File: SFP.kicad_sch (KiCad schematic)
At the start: 45 parts, among them J6 Bel-Fuse_SFP+_1x20_SS-79100-0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, U13 PCA9539AHF

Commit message: [#82757] Rename project to jetson-agx-thor-baseboard
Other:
- title: Jetson Orin AGX Baseboard -> Jetson AGX Thor Baseboard
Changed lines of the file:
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@@
 	(paper "A3")
 	(title_block
-		(title "Jetson Orin AGX Baseboard")
+		(title "Jetson AGX Thor Baseboard")
 		(date "2025-08-11")
 		(rev "1.0.0")

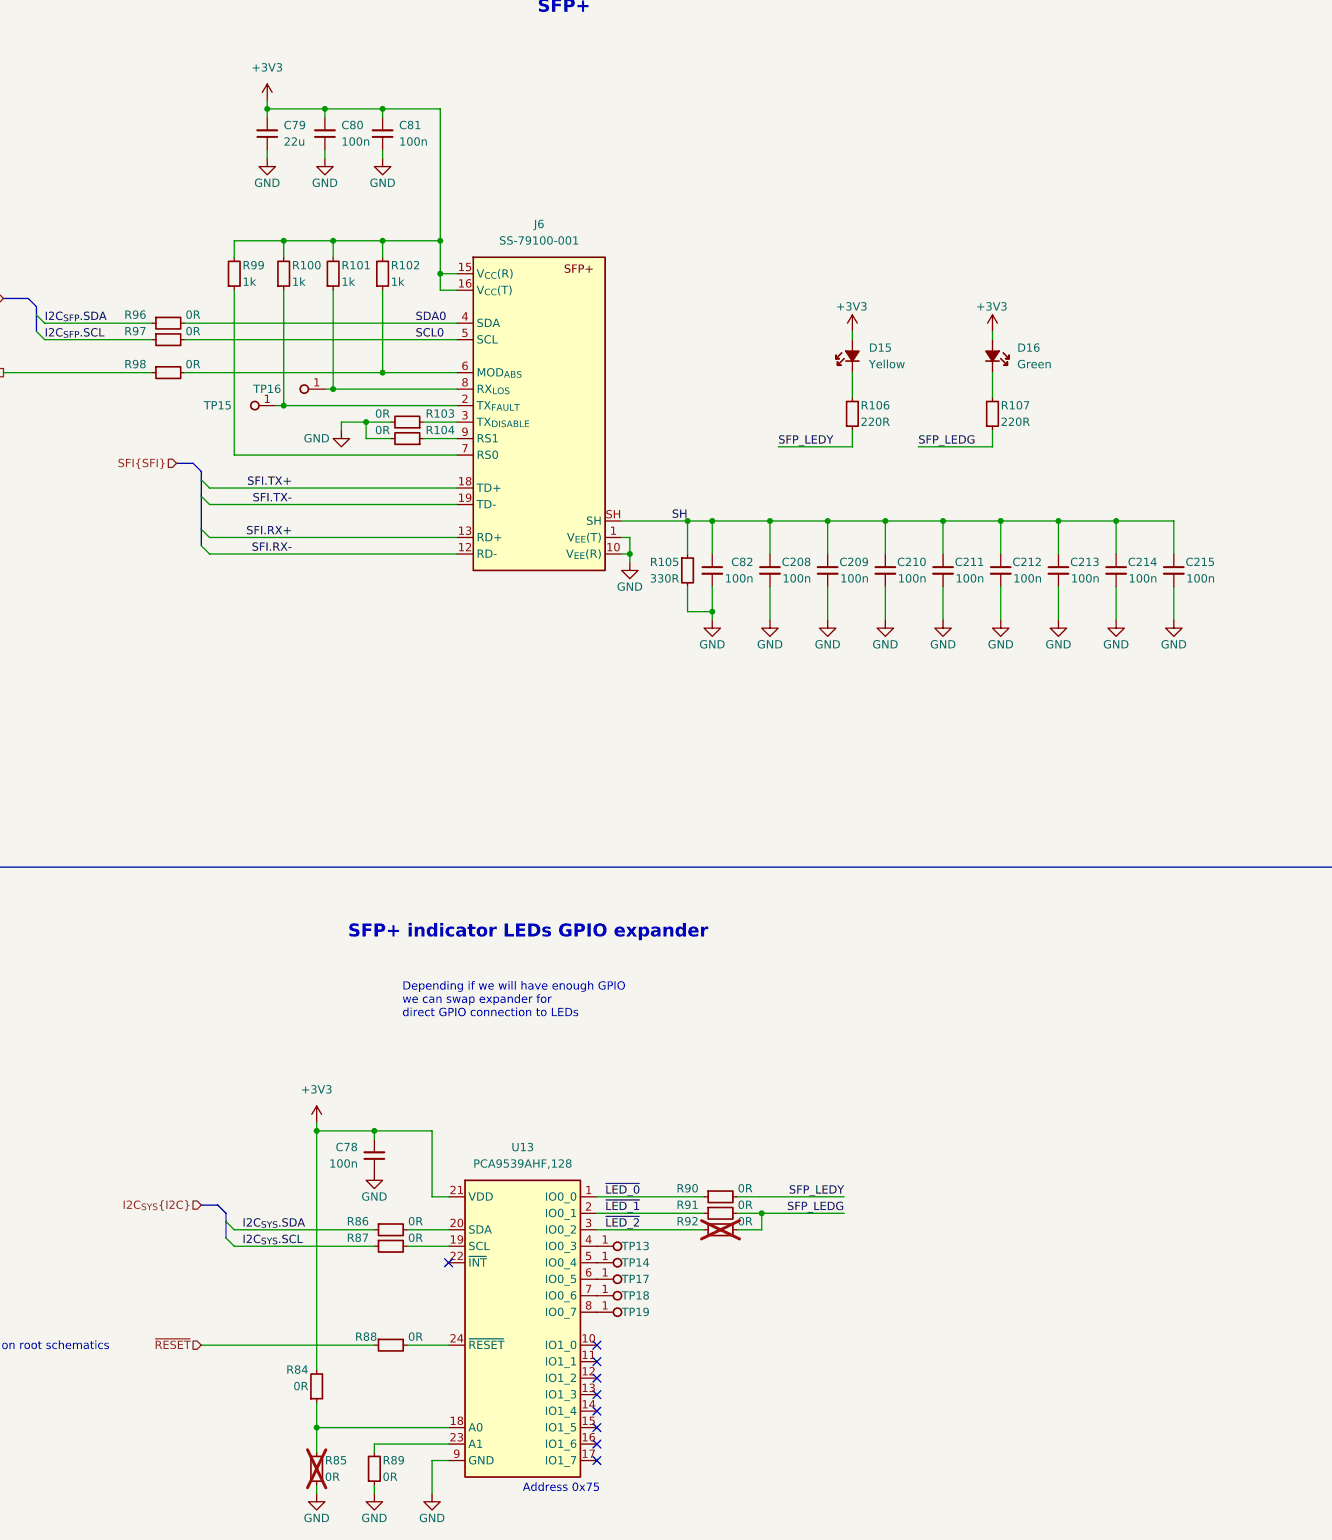
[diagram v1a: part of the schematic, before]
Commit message: [#82757] Cleanup: reorganise page numbers and fix annotations
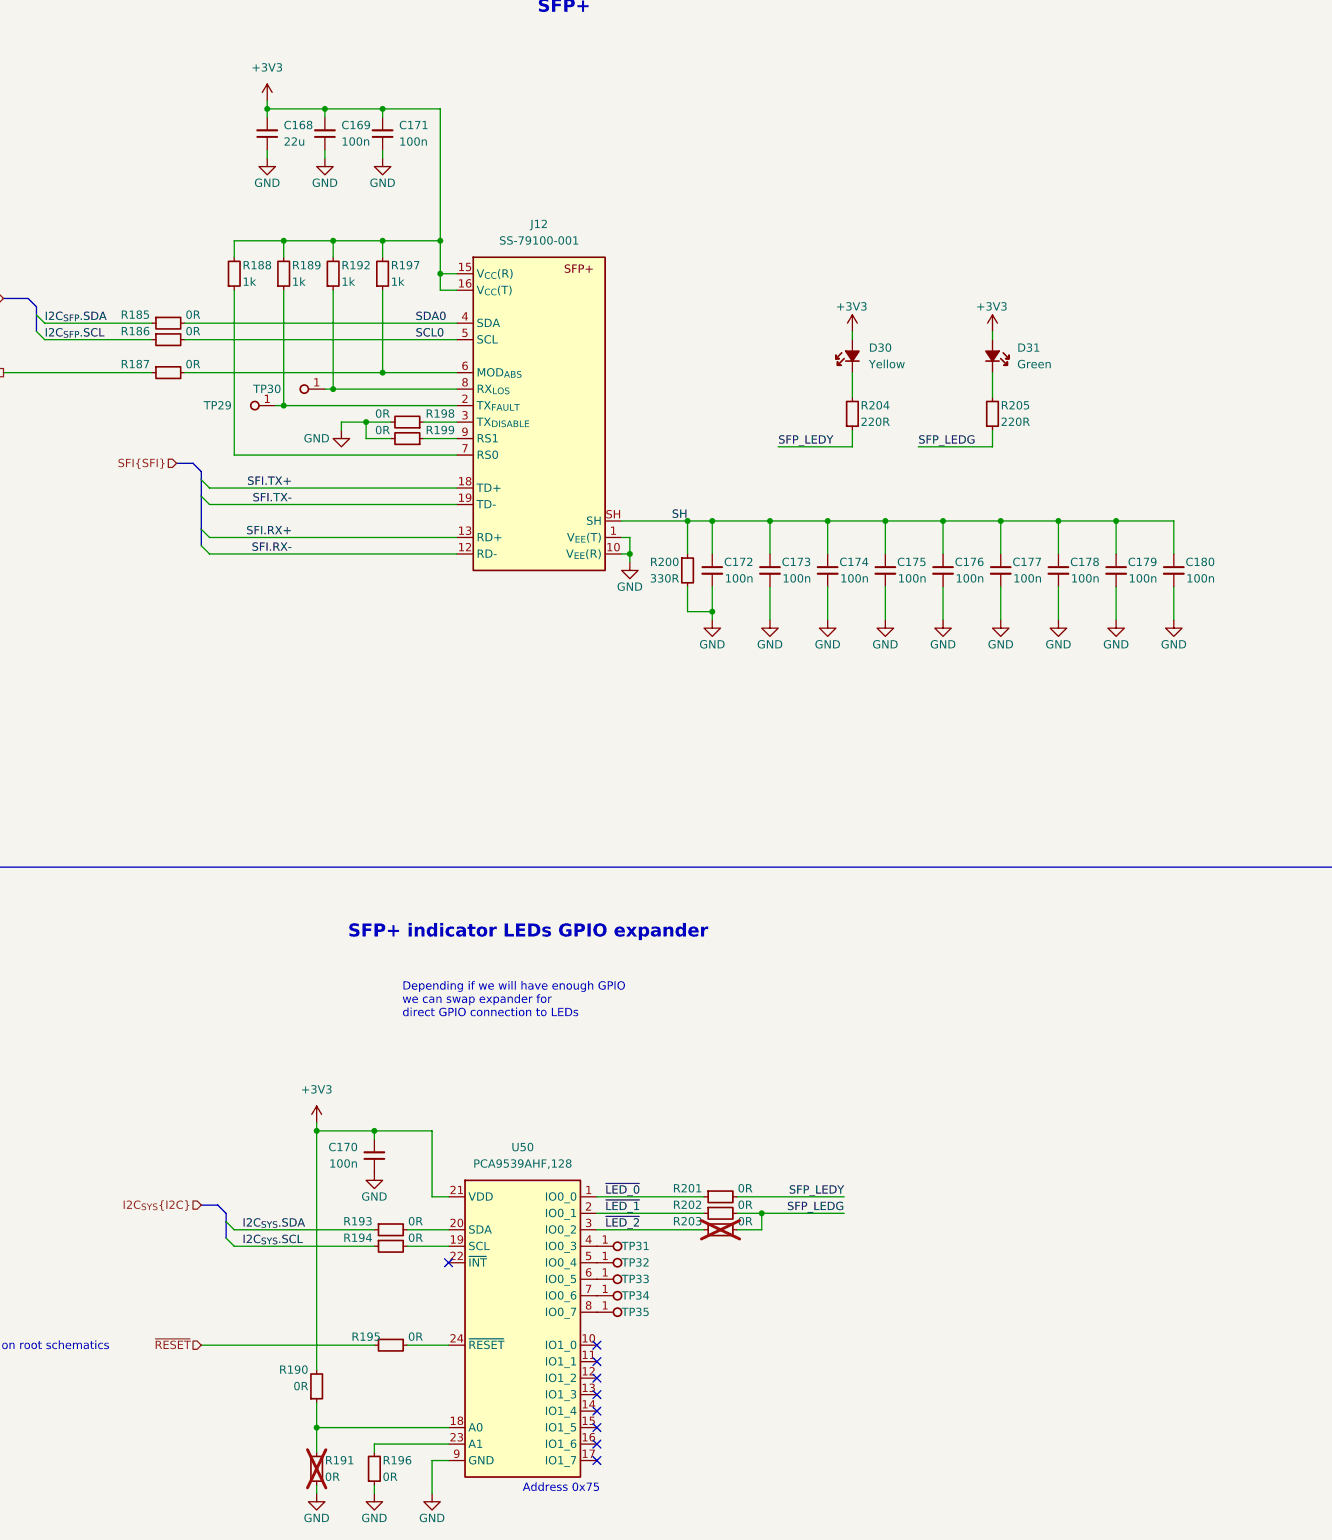
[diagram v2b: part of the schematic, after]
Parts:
- renumbered C79 to C168, C80 to C169, C78 to C170, C81 to C171, C82 to C172, C208 to C173, C209 to C174, C210 to C175, C211 to C176, C212 to C177, C213 to C178, C214 to C179, C215 to C180, D15 to D30, D16 to D31, J6 to J12, R96 to R185, R97 to R186, R98 to R187, R99 to R188, R100 to R189, R84 to R190, R85 to R191, R101 to R192, R86 to R193, R87 to R194, R88 to R195, R89 to R196, R102 to R197, R103 to R198, R104 to R199, R105 to R200, R90 to R201, R91 to R202, R92 to R203, R106 to R204, R107 to R205, TP15 to TP29, TP16 to TP30, TP13 to TP31, TP14 to TP32, TP17 to TP33, TP18 to TP34, TP19 to TP35, U13 to U50
